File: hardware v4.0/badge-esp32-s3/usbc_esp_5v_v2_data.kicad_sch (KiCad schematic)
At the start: 22 parts, among them J2 Connector, USB-TYPE-C-16P, Q10 AO3424, U11 SY6288F1ABC, U12 SY6288F1ABC, U8 TUSB321AIRWBR

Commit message: finished schematics and layout
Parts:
- removed D16: SS32F_C719168, lcsc-lib:SMAF_L3.5-W2.6-LS4.7-RD, symbol lcsc-lib:SS32F_C719168
- removed D9: BAT54W_C7502705, lcsc-lib:SOD-123_L2.7-W1.6-LS3.7-RD, symbol lcsc-lib:BAT54W_C7502705
- removed Q10: AO3424, lcsc-lib:SC-59-3_L2.9-W1.6-P0.95-LS2.9-BR, symbol lcsc-lib:AO3424
- removed R64, R65: 10kΩ, PCM_JLCPCB:R_0402, symbol PCM_JLCPCB-Resistors:0402,10kΩ
- removed R67: 6.8kΩ, PCM_JLCPCB:R_0402, symbol PCM_JLCPCB-Resistors:0402,6.8kΩ
- removed R68: 13kΩ, PCM_JLCPCB:R_0603, symbol PCM_JLCPCB-Resistors:0603,13kΩ
- added D10: B5819WT, PCM_JLCPCB:D_SOD-523, symbol PCM_JLCPCB-Diodes:Schottky,B5819WT
- added D16: B0520W, PCM_JLCPCB:D_SOD-123, symbol PCM_JLCPCB-Diodes:Schottky,B0520W
- added D18: SS32F_C719168, lcsc-lib:SMAF_L3.5-W2.6-LS4.7-RD, symbol lcsc-lib:SS32F_C719168
- added D19: Red, PCM_JLCPCB:D_0603, symbol PCM_JLCPCB-Diodes:LED,0603,Red
- added Q3: AP1606, lcsc-lib:DFN-3L_L1.0-W0.6-P0.65-BR, symbol lcsc-lib:AP1606
- added R61: 3.3kΩ, PCM_JLCPCB:R_0402, symbol PCM_JLCPCB-Resistors:0402,3.3kΩ
- added R64: 330Ω, PCM_JLCPCB:R_0402, symbol PCM_JLCPCB-Resistors:0402,330Ω
- added R65: 12kΩ, PCM_JLCPCB:R_0402, symbol PCM_JLCPCB-Resistors:0402,12kΩ
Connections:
- net GND: now also Q3.2 (S), R61.2, R65.2
- net USB_ID: now also D10.1, D19.1
- net USB_SINK_EN: now also D10.2
- net USB_SOURCE_EN: now also Q3.3 (D)
- net at U11.1 (OUT): now also D16.2, D18.2 (A)
- net at U11.5 (ISET): now also R61.1
- net at R66.2: now also Q3.1 (G)
- net at U12.5 (ISET): now also R65.1
- net Boost_5V renamed 5V_stable
- net 5V_stable: now also R64.1
- new net: D19.2, R64.2
- new net USB_RAW_HighCurrent: D18.1 (K)
- new net USB_RAW_LowCurrent: D16.1
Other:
- note added: "Active High (default: OFF)"
- note added: "Active High (default: ON)"
- note added: "By default Sinking current is enabled and Sourcing current is disabled"
- note added: "ISET: 0.57A"
- note added: "ISET: 2.1A"
- note added: "USB Power Sourcing Mode Indicator LED"
- note removed: "Active High (default: OFF - pulled down)"
- note removed: "Active High (default: ON - pulled up)"
- note removed: "By default Sinking current is enabled and Sourcing curreing is disabled"
- note removed: "ISET: 0.52A"
- note removed: "ISET: 2A"
- note removed: "USB_ID: Input to MCU HIGH when providing power (downstream device is power sink) LOW when recieving power (downstream device is power source)"
- moved on the sheet: C4

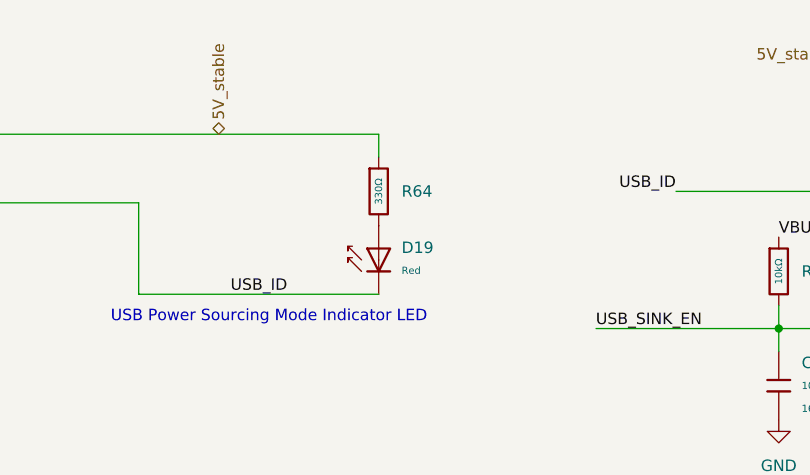
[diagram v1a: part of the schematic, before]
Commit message: changed buzzer pot
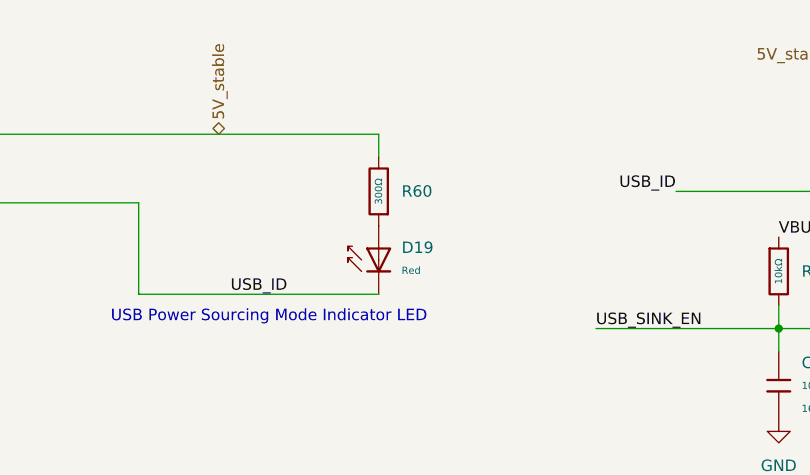
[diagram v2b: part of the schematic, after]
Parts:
- removed R64: 330Ω, PCM_JLCPCB:R_0402, symbol PCM_JLCPCB-Resistors:0402,330Ω
- added R60: 300Ω, PCM_JLCPCB:R_0402, symbol PCM_JLCPCB-Resistors:0402,300Ω
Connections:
- net 5V_stable: now also R60.2
- net at D19.2: now also R60.1
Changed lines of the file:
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@@
 		(polyline
 			(pts
-				(xy 17.78 74.93) (xy 238.76 74.93) (xy 238.76 161.29) (xy 17.78 161.29)
+				(xy 177.8 19.05) (xy 280.67 19.05) (xy 280.67 68.58) (xy 177.8 68.58)
 			)
 			(stroke
@@
 		(polyline
 			(pts
-				(xy 177.8 19.05) (xy 280.67 19.05) (xy 280.67 68.58) (xy 177.8 68.58)
+				(xy 17.78 19.05) (xy 172.72 19.05) (xy 172.72 68.58) (xy 17.78 68.58)
 			)
 			(stroke
@@
 		(polyline
 			(pts
-				(xy 17.78 19.05) (xy 172.72 19.05) (xy 172.72 68.58) (xy 17.78 68.58)
+				(xy 17.78 74.93) (xy 238.76 74.93) (xy 238.76 161.29) (xy 17.78 161.29)
 			)
 			(stroke
@@
 	)
 	(symbol
-		(lib_id "PCM_JLCPCB-Resistors:0402,330Ω")
-		(at 160.02 36.83 0)
-		(unit 1)
-		(exclude_from_sim no)
-		(in_bom yes)
-		(on_board yes)
-		(dnp no)
-		(fields_autoplaced yes)
-		(property "Reference" "R64"
-			(at 162.56 36.8299 0)
-			(effects
-				(font
-					(size 1.27 1.27)
-				)
-				(justify left)
-			)
-		)
-		(property "Value" "330Ω"
-			(at 160.02 36.83 90)
-			(do_not_autoplace yes)
-			(effects
-				(font
-					(size 0.8 0.8)
-				)
-			)
-		)
-		(property "Footprint" "PCM_JLCPCB:R_0402"
-			(at 158.242 36.83 90)
-			(effects
-				(font
-					(size 1.27 1.27)
-				)
-				(hide yes)
-			)
-		)
-		(property "Datasheet" "https://www.lcsc.com/datasheet/lcsc_datasheet_2205311900_UNI-ROYAL-Uniroyal-Elec-0402WGF3300TCE_C25104.pdf"
-			(at 160.02 36.83 0)
-			(effects
-				(font
-					(size 1.27 1.27)
-				)
-				(hide yes)
-			)
-		)
-		(property "Description" "62.5mW Thick Film Resistors 50V ±100ppm/°C ±1% 330Ω 0402 Chip Resistor - Surface Mount ROHS"
-			(at 160.02 36.83 0)
-			(effects
-				(font
-					(size 1.27 1.27)
-				)
-				(hide yes)
-			)
-		)
-		(property "LCSC" "C25104"
-			(at 160.02 36.83 0)
-			(effects
-				(font
-					(size 1.27 1.27)
-				)
-				(hide yes)
-			)
-		)
-		(property "Stock" "1159127"
-			(at 160.02 36.83 0)
-			(effects
-				(font
-					(size 1.27 1.27)
-				)
-				(hide yes)
-			)
-		)
-		(property "Price" "0.004USD"
-			(at 160.02 36.83 0)
-			(effects
-				(font
-					(size 1.27 1.27)
-				)
-				(hide yes)
-			)
-		)
-		(property "Process" "SMT"
-			(at 160.02 36.83 0)
-			(effects
-				(font
-					(size 1.27 1.27)
-				)
-				(hide yes)
-			)
-		)
-		(property "Minimum Qty" "20"
-			(at 160.02 36.83 0)
-			(effects
-				(font
-					(size 1.27 1.27)
-				)
-				(hide yes)
-			)
-		)
-		(property "Attrition Qty" "10"
-			(at 160.02 36.83 0)
-			(effects
-				(font
-					(size 1.27 1.27)
-				)
-				(hide yes)
-			)
-		)
-		(property "Class" "Basic Component"
-			(at 160.02 36.83 0)
-			(effects
-				(font
-					(size 1.27 1.27)
-				)
-				(hide yes)
-			)
-		)
-		(property "Category" "Resistors,Chip Resistor - Surface Mount"
-			(at 160.02 36.83 0)
-			(effects
-				(font
-					(size 1.27 1.27)
-				)
-				(hide yes)
-			)
-		)
-		(property "Manufacturer" "UNI-ROYAL(Uniroyal Elec)"
-			(at 160.02 36.83 0)
-			(effects
-				(font
-					(size 1.27 1.27)
-				)
-				(hide yes)
-			)
-		)
-		(property "Part" "0402WGF3300TCE"
-			(at 160.02 36.83 0)
-			(effects
-				(font
-					(size 1.27 1.27)
-				)
-				(hide yes)
-			)
-		)
-		(property "Resistance" "330Ω"
-			(at 160.02 36.83 0)
-			(effects
-				(font
-					(size 1.27 1.27)
-				)
-				(hide yes)
-			)
-		)
-		(property "Power(Watts)" "62.5mW"
-			(at 160.02 36.83 0)
-			(effects
-				(font
-					(size 1.27 1.27)
-				)
-				(hide yes)
-			)
-		)
-		(property "Type" "Thick Film Resistors"
-			(at 160.02 36.83 0)
-			(effects
-				(font
-					(size 1.27 1.27)
-				)
-				(hide yes)
-			)
-		)
-		(property "Overload Voltage (Max)" "50V"
-			(at 160.02 36.83 0)
-			(effects
-				(font
-					(size 1.27 1.27)
-				)
-				(hide yes)
-			)
-		)
-		(property "Operating Temperature Range" "-55°C~+155°C"
-			(at 160.02 36.83 0)
-			(effects
-				(font
-					(size 1.27 1.27)
-				)
-				(hide yes)
-			)
-		)
-		(property "Tolerance" "±1%"
-			(at 160.02 36.83 0)
-			(effects
-				(font
-					(size 1.27 1.27)
-				)
-				(hide yes)
-			)
-		)
-		(property "Temperature Coefficient" "±100ppm/°C"
-			(at 160.02 36.83 0)
-			(effects
-				(font
-					(size 1.27 1.27)
-				)
-				(hide yes)
-			)
-		)
-		(pin "1"
-		)
-		(pin "2"
-		)
-		(instances
-			(project ""
-				(path "/e2af9a6c-dbe9-4de2-9ba6-ea213a7300ec/791664b9-b2ed-4f3b-9466-1f499155c51d"
-					(reference "R64")
-					(unit 1)
-				)
-			)
-		)
-	)
-	(symbol
 		(lib_id "power:GND")
 		(at 58.42 48.26 0)
@@
 					(unit 1)
 				)
+			)
+		)
+	)
+	(symbol
+		(lib_id "PCM_JLCPCB-Resistors:0402,300Ω")
+		(at 160.02 36.83 180)
+		(unit 1)
+		(exclude_from_sim no)
+		(in_bom yes)
+		(on_board yes)
+		(dnp no)
+		(fields_autoplaced yes)
+		(property "Reference" "R60"
+			(at 162.56 36.8299 0)
+			(effects
+				(font
+					(size 1.27 1.27)
+				)
+				(justify right)
+			)
+		)
+		(property "Value" "300Ω"
+			(at 160.02 36.83 90)
+			(do_not_autoplace yes)
+			(effects
+				(font
+					(size 0.8 0.8)
+				)
+			)
+		)
+		(property "Footprint" "PCM_JLCPCB:R_0402"
+			(at 161.798 36.83 90)
+			(effects
+				(font
+					(size 1.27 1.27)
+				)
+				(hide yes)
+			)
+		)
+		(property "Datasheet" "https://www.lcsc.com/datasheet/lcsc_datasheet_2205311900_UNI-ROYAL-Uniroyal-Elec-0402WGF3000TCE_C25102.pdf"
+			(at 160.02 36.83 0)
+			(effects
+				(font
+					(size 1.27 1.27)
+				)
+				(hide yes)
+			)
+		)
+		(property "Description" "62.5mW Thick Film Resistors 50V ±100ppm/°C ±1% 300Ω 0402 Chip Resistor - Surface Mount ROHS"
+			(at 160.02 36.83 0)
+			(effects
+				(font
+					(size 1.27 1.27)
+				)
+				(hide yes)
+			)
+		)
+		(property "LCSC" "C25102"
+			(at 160.02 36.83 0)
+			(effects
+				(font
+					(size 1.27 1.27)
+				)
+				(hide yes)
+			)
+		)
+		(property "Stock" "234904"
+			(at 160.02 36.83 0)
+			(effects
+				(font
+					(size 1.27 1.27)
+				)
+				(hide yes)
+			)
+		)
+		(property "Price" "0.004USD"
+			(at 160.02 36.83 0)
+			(effects
+				(font
+					(size 1.27 1.27)
+				)
+				(hide yes)
+			)
+		)
+		(property "Process" "SMT"
+			(at 160.02 36.83 0)
+			(effects
+				(font
+					(size 1.27 1.27)
+				)
+				(hide yes)
+			)
+		)
+		(property "Minimum Qty" "20"
+			(at 160.02 36.83 0)
+			(effects
+				(font
+					(size 1.27 1.27)
+				)
+				(hide yes)
+			)
+		)
+		(property "Attrition Qty" "10"
+			(at 160.02 36.83 0)
+			(effects
+				(font
+					(size 1.27 1.27)
+				)
+				(hide yes)
+			)
+		)
+		(property "Class" "Preferred Component"
+			(at 160.02 36.83 0)
+			(effects
+				(font
+					(size 1.27 1.27)
+				)
+				(hide yes)
+			)
+		)
+		(property "Category" "Resistors,Chip Resistor - Surface Mount"
+			(at 160.02 36.83 0)
+			(effects
+				(font
+					(size 1.27 1.27)
+				)
+				(hide yes)
+			)
+		)
+		(property "Manufacturer" "UNI-ROYAL(Uniroyal Elec)"
+			(at 160.02 36.83 0)
+			(effects
+				(font
+					(size 1.27 1.27)
+				)
+				(hide yes)
+			)
+		)
+		(property "Part" "0402WGF3000TCE"
+			(at 160.02 36.83 0)
+			(effects
+				(font
+					(size 1.27 1.27)
+				)
+				(hide yes)
+			)
+		)
+		(property "Resistance" "300Ω"
+			(at 160.02 36.83 0)
+			(effects
+				(font
+					(size 1.27 1.27)
+				)
+				(hide yes)
+			)
+		)
+		(property "Power(Watts)" "62.5mW"
+			(at 160.02 36.83 0)
+			(effects
+				(font
+					(size 1.27 1.27)
+				)
+				(hide yes)
+			)
+		)
+		(property "Type" "Thick Film Resistors"
+			(at 160.02 36.83 0)
+			(effects
+				(font
+					(size 1.27 1.27)
+				)
+				(hide yes)
+			)
+		)
+		(property "Overload Voltage (Max)" "50V"
+			(at 160.02 36.83 0)
+			(effects
+				(font
+					(size 1.27 1.27)
+				)
+				(hide yes)
+			)
+		)
+		(property "Operating Temperature Range" "-55°C~+155°C"
+			(at 160.02 36.83 0)
+			(effects
+				(font
+					(size 1.27 1.27)
+				)
+				(hide yes)
+			)
+		)
+		(property "Tolerance" "±1%"
+			(at 160.02 36.83 0)
+			(effects
+				(font
+					(size 1.27 1.27)
+				)
+				(hide yes)
+			)
+		)
+		(property "Temperature Coefficient" "±100ppm/°C"
+			(at 160.02 36.83 0)
+			(effects
+				(font
+					(size 1.27 1.27)
+				)
+				(hide yes)
+			)
+		)
+		(pin "1"
+		)
+		(pin "2"
+		)
+		(instances
+			(project "badge-esp32-s3"
+				(path "/e2af9a6c-dbe9-4de2-9ba6-ea213a7300ec/791664b9-b2ed-4f3b-9466-1f499155c51d"
+					(reference "R60")
+					(unit 1)
+				)
